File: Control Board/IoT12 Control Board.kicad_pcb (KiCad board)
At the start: 2 copper layers, 99.1 x 69.8 mm, 110 parts, among them J10 USB_B_Micro, J11 Conn_ARM_JTAG_SWD_10, J9 Conn_ARM_JTAG_SWD_10, Q1 MMBT2222, Q2 MMBT2222, Q3 AOD403, SW1 Rotary encoder EC11 Plum 15mm, SW2 SW_Push, U1 ATSAMD21G18A-AU, U2 ADS1115IDGS, U3 INA826AID, U4 INA826AID, U5 LM2596S-ADJ, U6 AT24C32, Y1 32768Hz

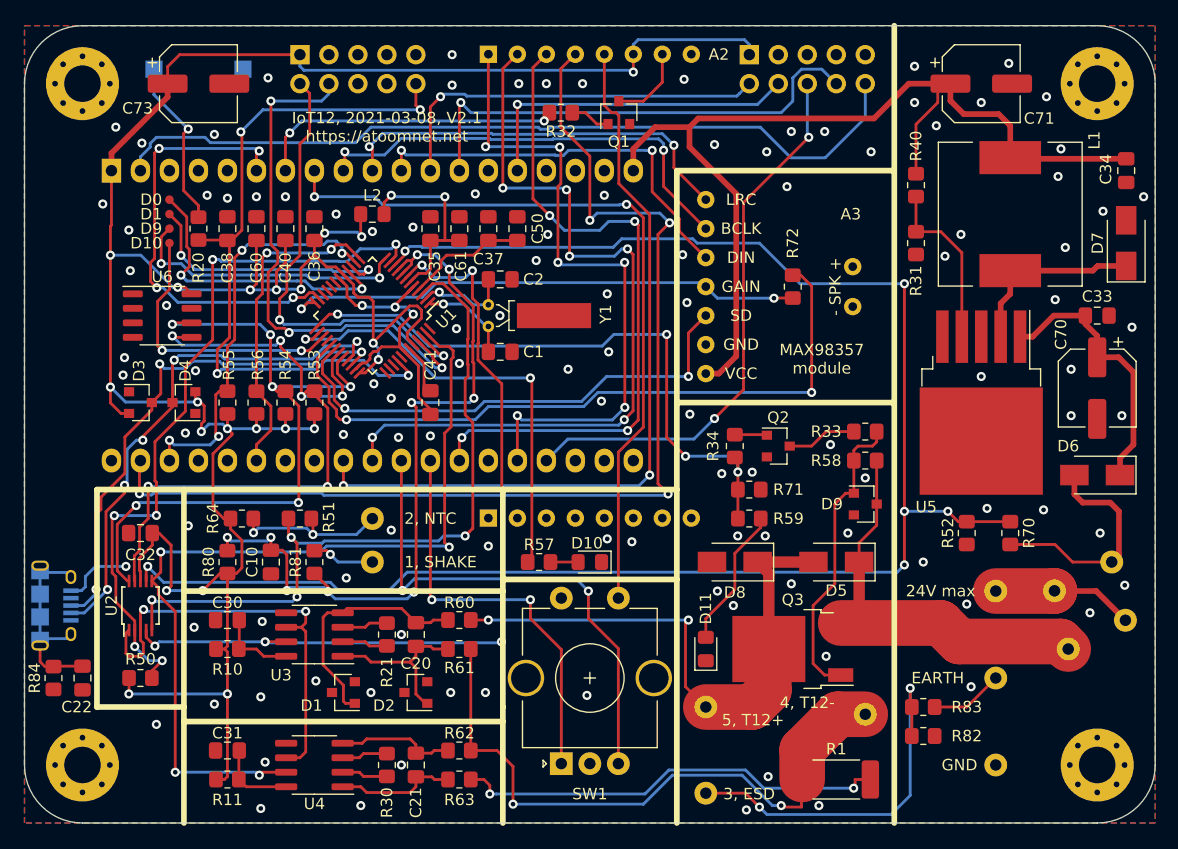
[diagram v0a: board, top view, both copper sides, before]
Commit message: Added I2C addresses to silkscreen and schematic.
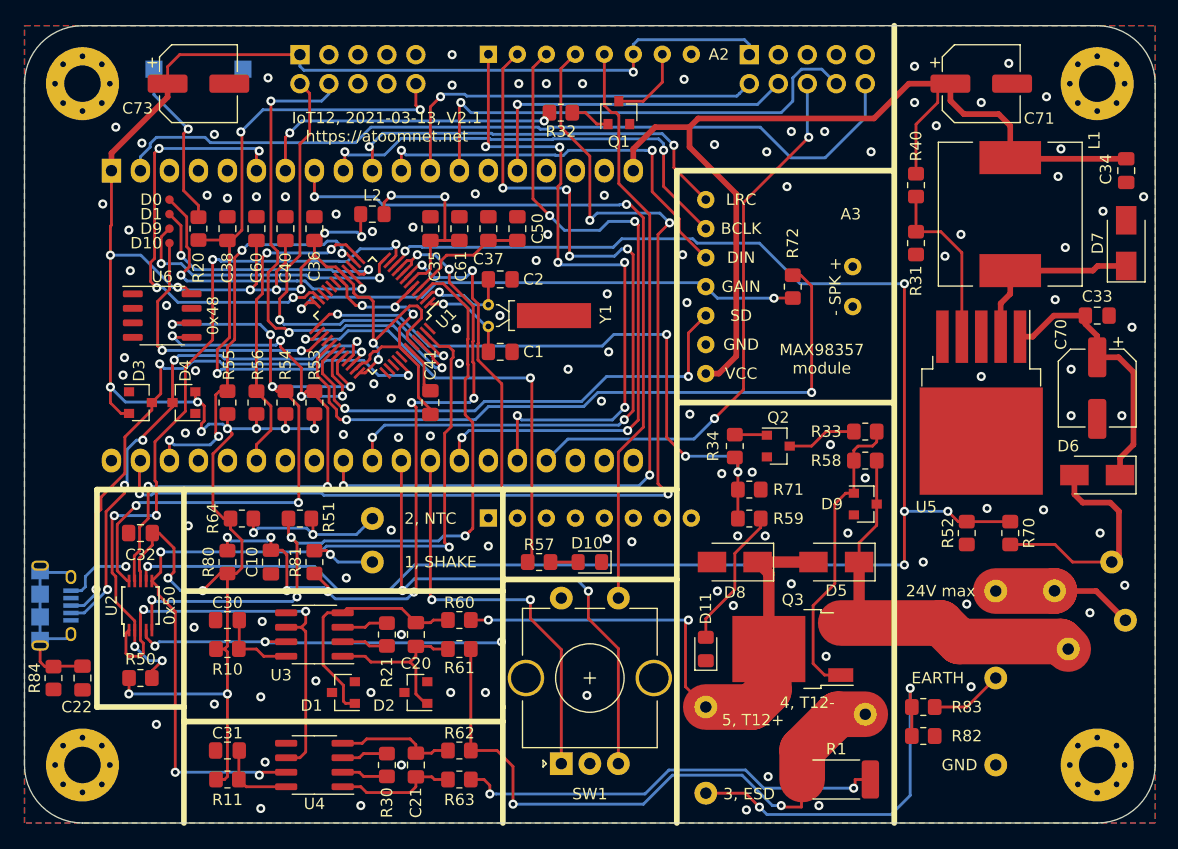
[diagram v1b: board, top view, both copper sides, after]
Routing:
- net +3V3: track 244.9 -> 244.3 mm
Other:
- board text added: "0x48"
- board text added: "0x50"
- board text added: "IoT12, 2021-03-13, V2.1 https://atoomnet.net"
- board text removed: "IoT12, 2021-03-08, V2.1 https://atoomnet.net"

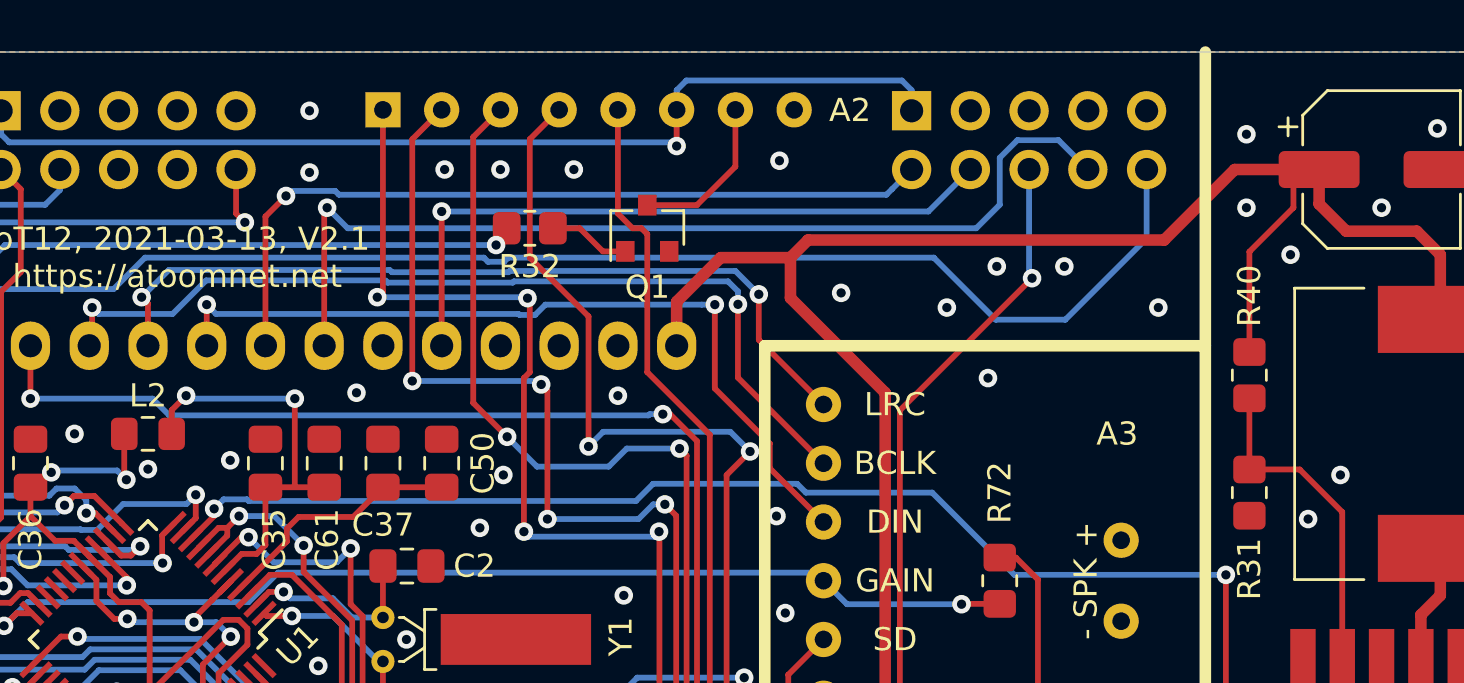
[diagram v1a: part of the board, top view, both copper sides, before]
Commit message: More testing and re-added voltage monitor.
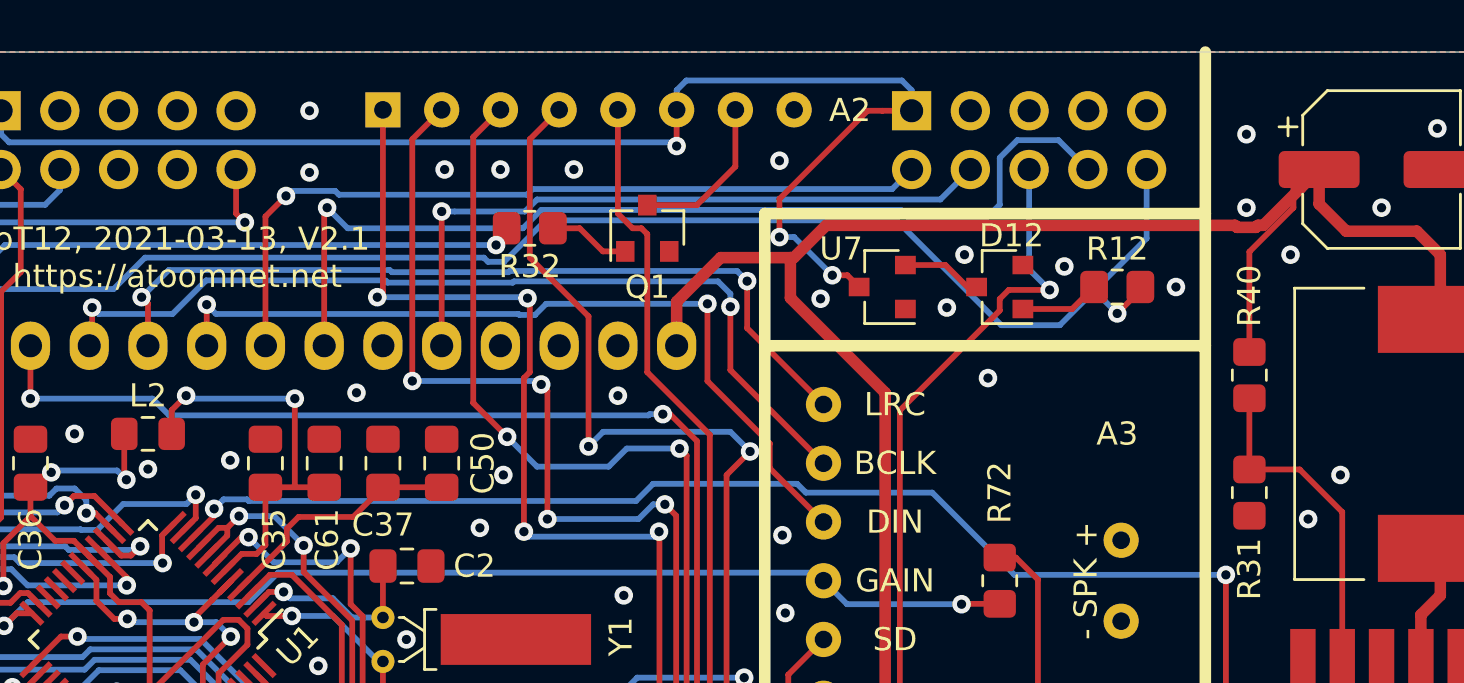
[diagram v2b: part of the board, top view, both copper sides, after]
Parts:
- added D12: BAV99, Package_TO_SOT_SMD:SOT-23, F.Cu at (17.8, -31.8)
- added R12: 100R, Resistor_SMD:R_0805_2012Metric_Pad1.20x1.40mm_HandSolder, F.Cu at (22.9, -31.8)
- added U7: MAX809S, Package_TO_SOT_SMD:SOT-23, F.Cu at (12.7, -31.8)
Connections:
- net EN renamed ESP32_~RESET
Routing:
- net +3V3: track 244.3 -> 257.6 mm, vias 21 -> 23
- net ESP32_~RESET: track 72.1 -> 76.5 mm, vias 0 -> 1
- net Net-(D12-Pad3): track 0.00 -> 3.47 mm
- net Net-(D12-Pad1): track 0.00 -> 3.47 mm
- net Net-(A1-Pad23): track 49.1 -> 50.7 mm

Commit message: Changed value R82.
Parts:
- R82: value 1M -> 4k7

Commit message: Updated revision date.
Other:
- board text added: "IoT12, 2021-03-27, V2.1 https://atoomnet.net"
- board text removed: "IoT12, 2021-03-13, V2.1 https://atoomnet.net"

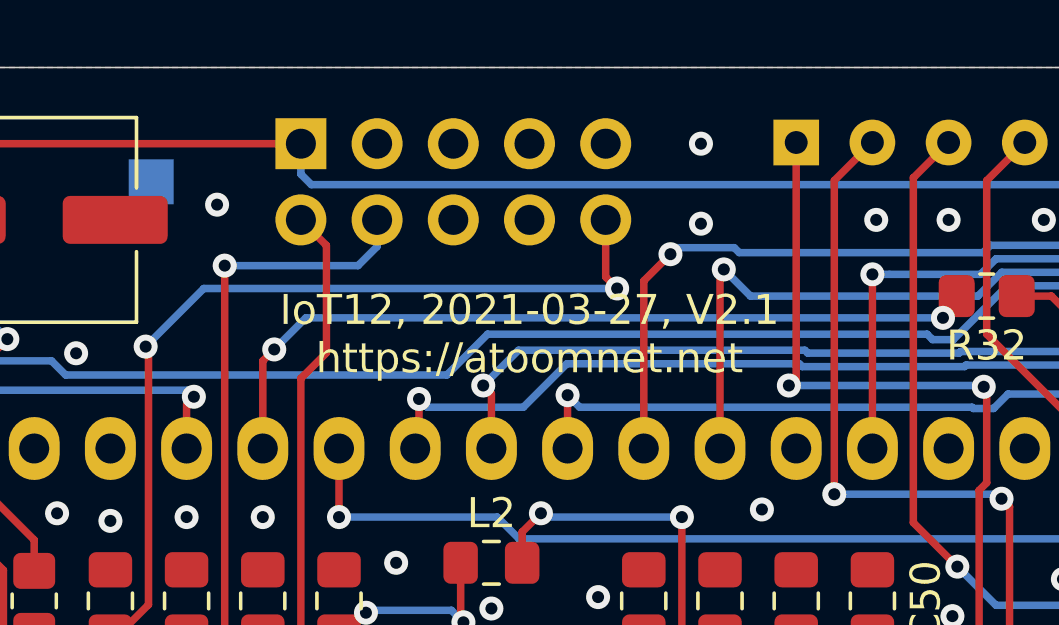
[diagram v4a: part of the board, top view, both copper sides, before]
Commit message: Revert R82 back to 1M.
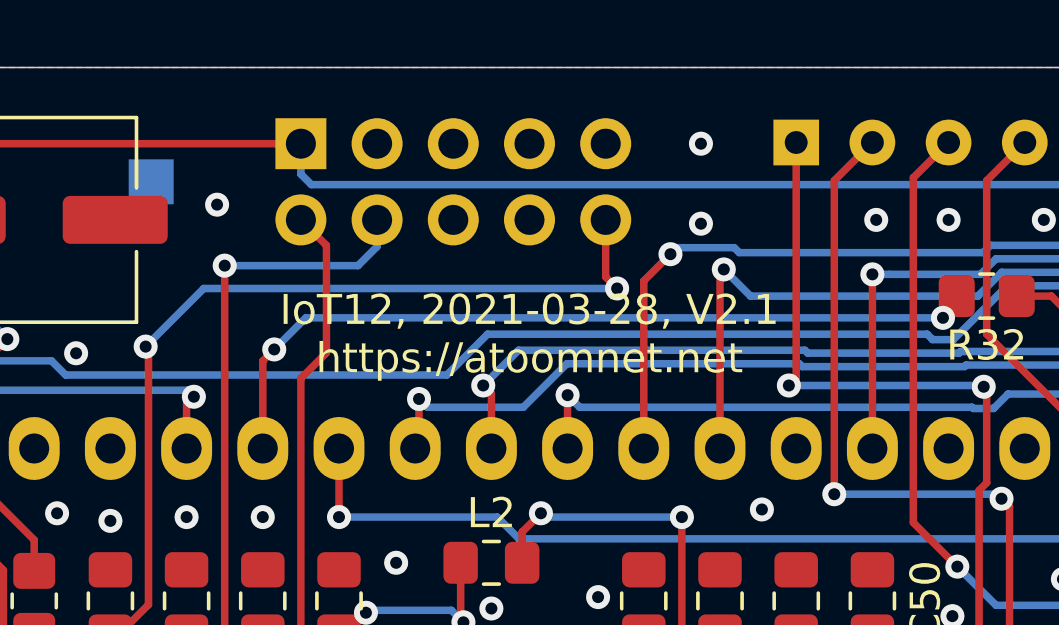
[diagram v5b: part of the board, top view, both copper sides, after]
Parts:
- R82: value 4k7 -> 1M
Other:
- board text added: "IoT12, 2021-03-28, V2.1 https://atoomnet.net"
- board text removed: "IoT12, 2021-03-27, V2.1 https://atoomnet.net"
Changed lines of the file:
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@@
   (page A4)
   (title_block
-    (date 2021-03-27)
+    (date 2021-03-28)
     (rev V2.1)
   )
@@
       (effects (font (size 1 1) (thickness 0.15)))
     )
-    (fp_text value 4k7 (at 0 1.65) (layer F.Fab)
+    (fp_text value 1M (at 0 1.65) (layer F.Fab)
       (effects (font (size 1 1) (thickness 0.15)))
     )
@@
     (effects (font (size 1 1) (thickness 0.15)) (justify mirror))
   )
-  (gr_text "IoT12, 2021-03-27, V2.1\nhttps://atoomnet.net" (at -17.78 -33.02) (layer F.SilkS)
+  (gr_text "IoT12, 2021-03-28, V2.1\nhttps://atoomnet.net" (at -17.78 -33.02) (layer F.SilkS)
     (effects (font (size 1 1) (thickness 0.15)))
   )

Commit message: V2.1 changes.
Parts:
- F1: value 2.5A/30V -> *see schematic.
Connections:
- R70 pad 2: Net-(D6-Pad2) -> +24V
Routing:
- net +24V: track 36.4 -> 46.6 mm
- net Net-(D6-Pad2): track 20.4 -> 10.9 mm
- net GND: vias 116 -> 117

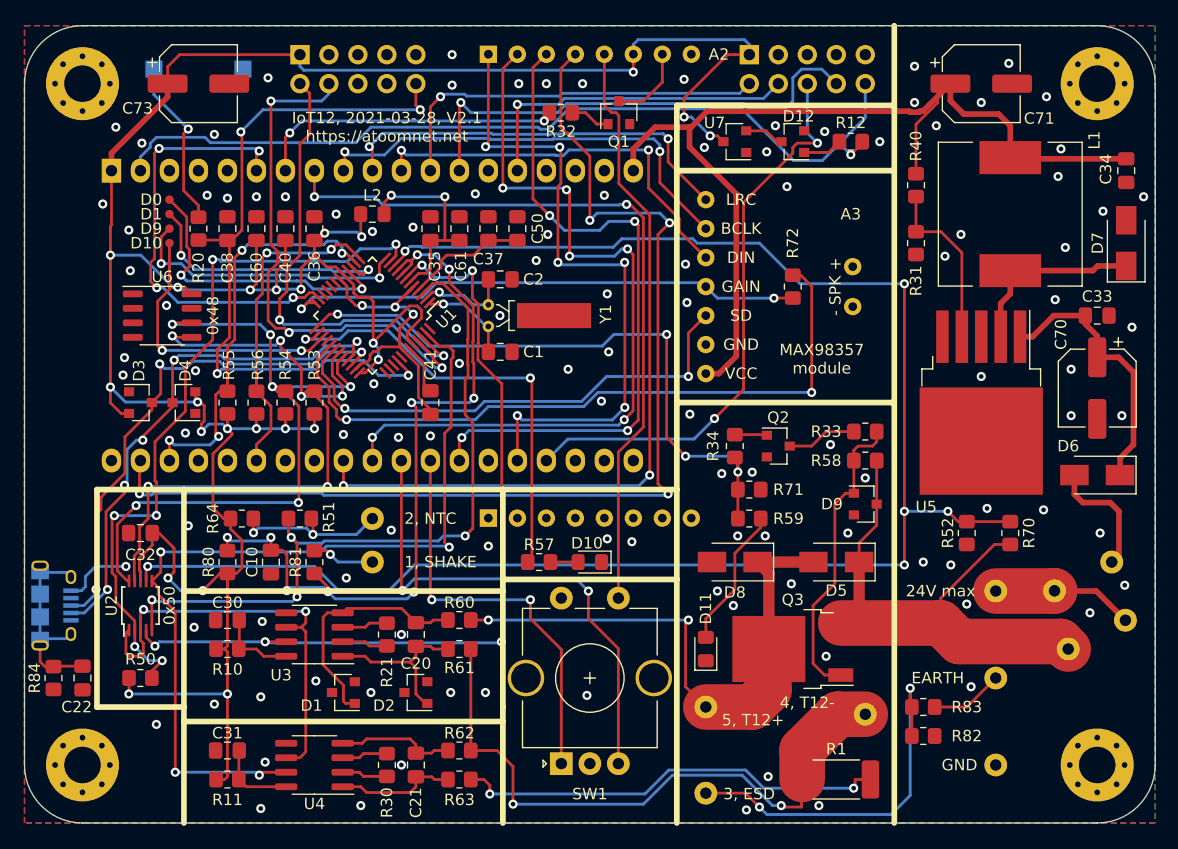
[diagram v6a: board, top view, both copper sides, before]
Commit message: Added ~RESET pulldown resistor.
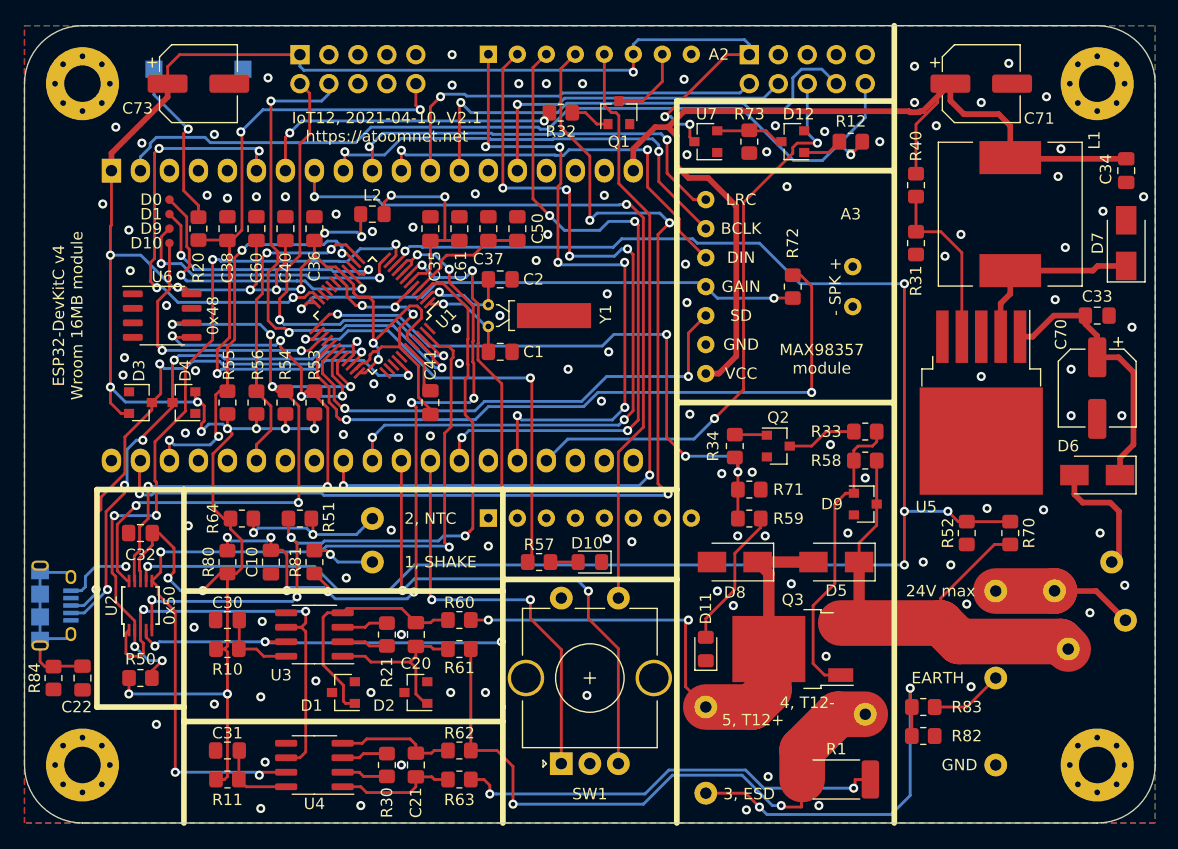
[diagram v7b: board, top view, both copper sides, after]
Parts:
- added R73: 100K, Resistor_SMD:R_0805_2012Metric_Pad1.20x1.40mm_HandSolder, F.Cu at (14.0, -31.8)
- moved U7 2.54 mm to (10.2, -31.8)
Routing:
- net Net-(D12-Pad3): track 3.47 -> 6.30 mm
- net +5V: track 86.5 -> 88.3 mm
- net I2S_WS: track 35.8 -> 36.3 mm
- net +3V3: track 257.6 -> 258.1 mm
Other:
- board text added: "ESP32-DevKitC v4 Wroom 16MB module"
- board text added: "IoT12, 2021-04-10, V2.1 https://atoomnet.net"
- board text removed: "ESP32-DevKitC module"
- board text removed: "IoT12, 2021-03-28, V2.1 https://atoomnet.net"
